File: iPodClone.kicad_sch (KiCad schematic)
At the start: 6 parts, among them U1 V3S, U4 AI12, U5 10104110-0001LF

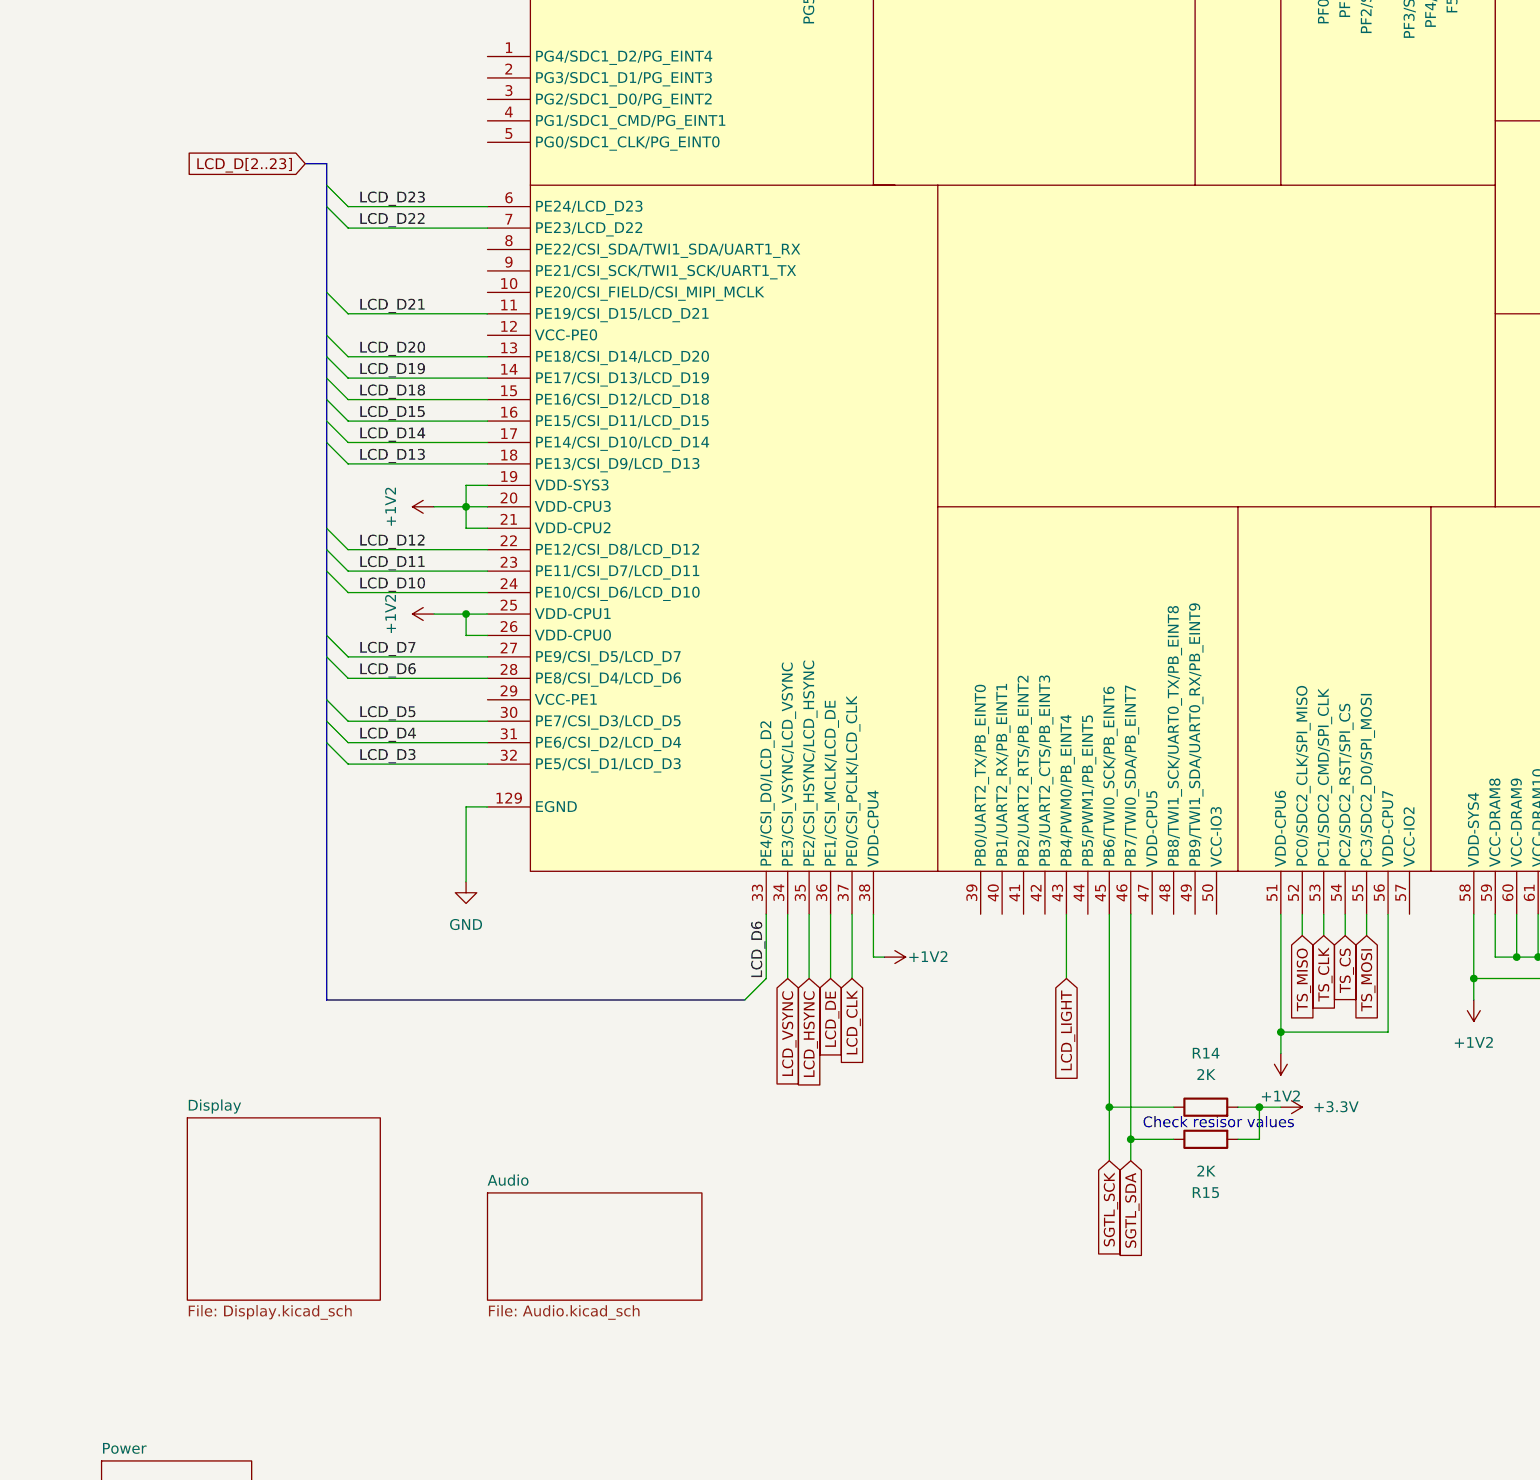
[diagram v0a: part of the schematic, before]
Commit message: power changes, audio changes, testing layout
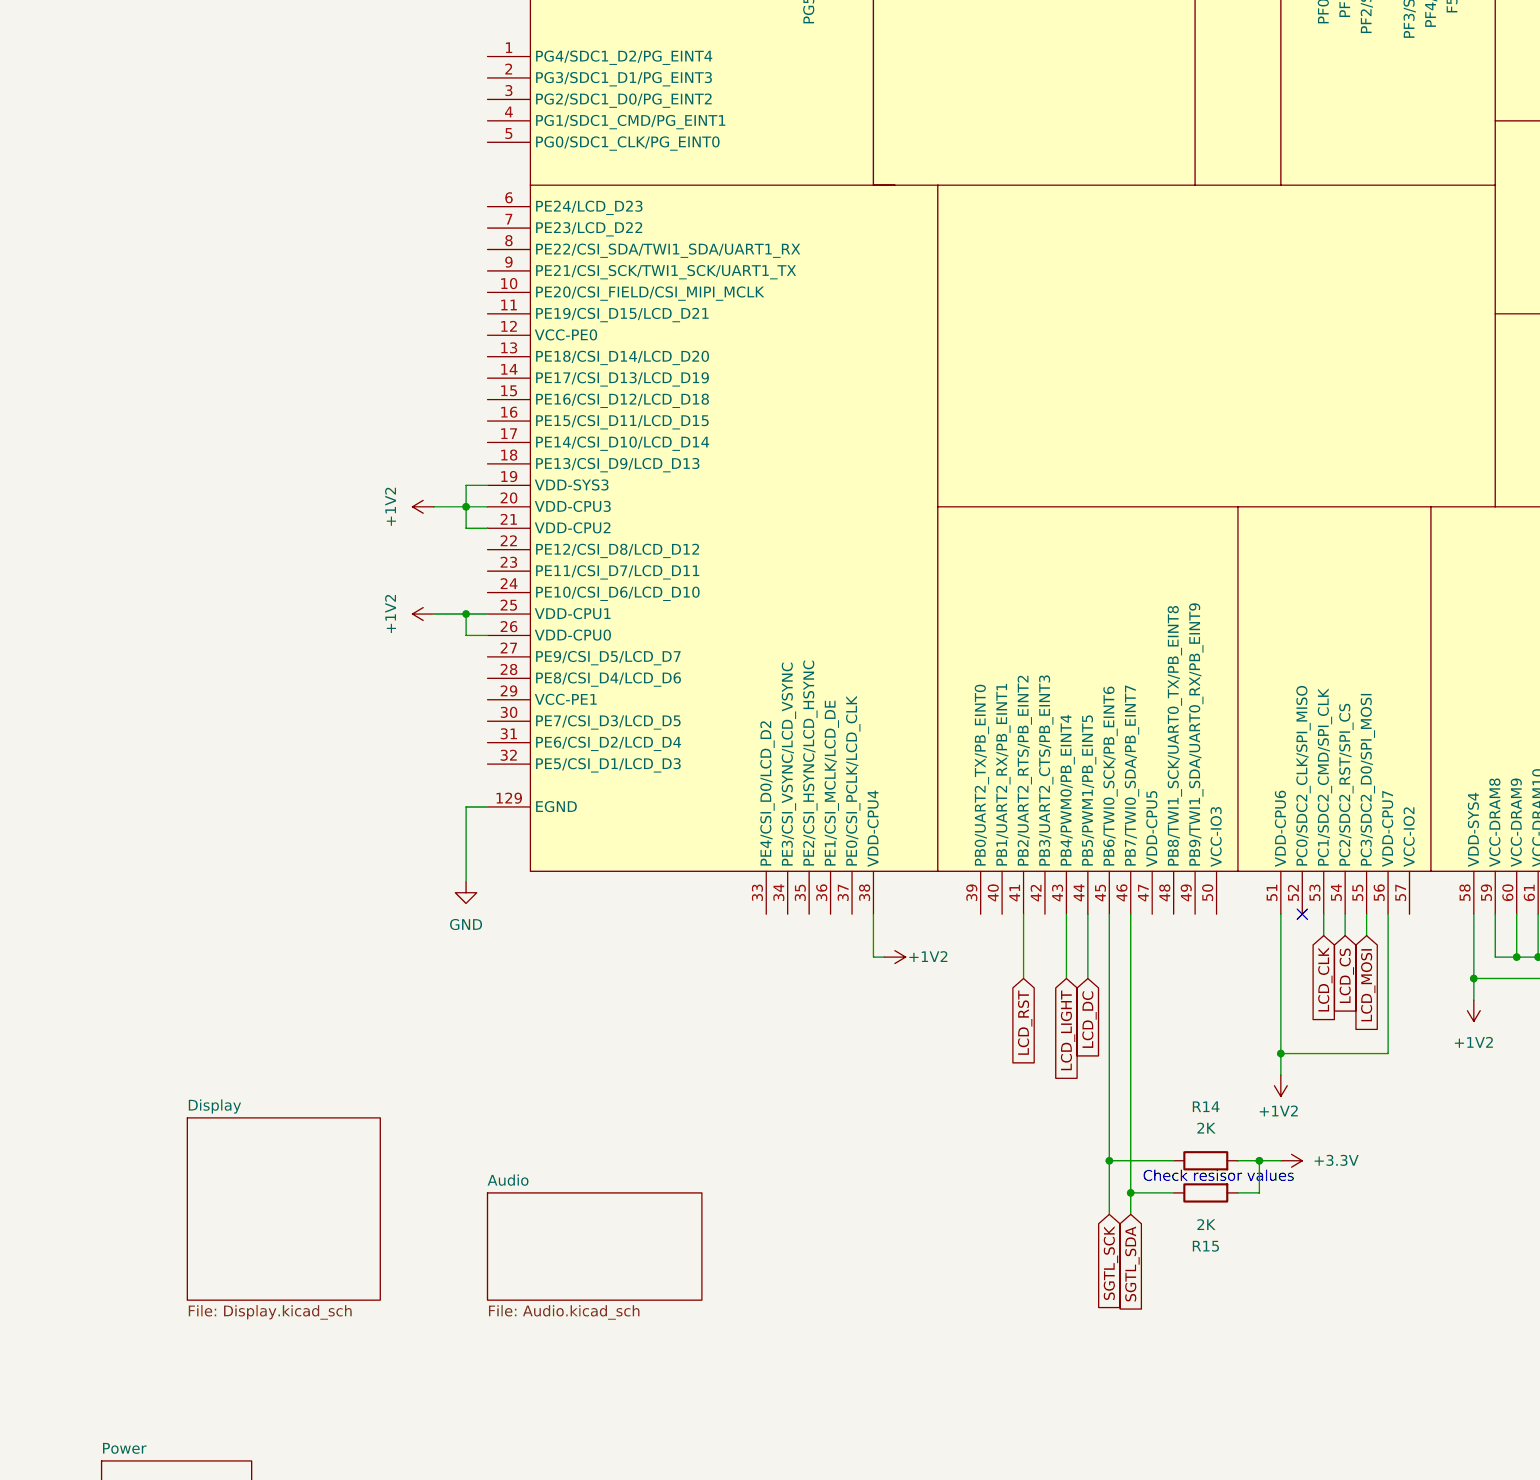
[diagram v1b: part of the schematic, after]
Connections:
- net TS_CLK is gone; now on net LCD_CLK: U1.53 (PC1/SDC2_CMD/SPI_CLK)
- net LCD_CLK: no longer U1.37 (PE0/CSI_PCLK/LCD_CLK)
- net LCD_RST: now reaches U1.41 (PB2/UART2_RTS/PB_EINT2)
- net LCD_DC: now reaches U1.44 (PB5/PWM1/PB_EINT5)
- net LCD_D10: no longer names the net of U1.24 (PE10/CSI_D6/LCD_D10)
- net LCD_D11: no longer names the net of U1.23 (PE11/CSI_D7/LCD_D11)
- net LCD_D12: no longer names the net of U1.22 (PE12/CSI_D8/LCD_D12)
- net LCD_D13: no longer names the net of U1.18 (PE13/CSI_D9/LCD_D13)
- net LCD_D14: no longer names the net of U1.17 (PE14/CSI_D10/LCD_D14)
- net LCD_D15: no longer names the net of U1.16 (PE15/CSI_D11/LCD_D15)
- net LCD_D18: no longer names the net of U1.15 (PE16/CSI_D12/LCD_D18)
- net LCD_D19: no longer names the net of U1.14 (PE17/CSI_D13/LCD_D19)
- net LCD_D20: no longer names the net of U1.13 (PE18/CSI_D14/LCD_D20)
- net LCD_D21: no longer names the net of U1.11 (PE19/CSI_D15/LCD_D21)
- net LCD_D22: no longer names the net of U1.7 (PE23/LCD_D22)
- net LCD_D23: no longer names the net of U1.6 (PE24/LCD_D23)
- net LCD_D3: no longer names the net of U1.32 (PE5/CSI_D1/LCD_D3)
- net LCD_D4: no longer names the net of U1.31 (PE6/CSI_D2/LCD_D4)
- net LCD_D5: no longer names the net of U1.30 (PE7/CSI_D3/LCD_D5)
- net LCD_D6: no longer names the net of U1.28 (PE8/CSI_D4/LCD_D6)
- net LCD_D6: no longer U1.33 (PE4/CSI_D0/LCD_D2)
- net LCD_D7: no longer names the net of U1.27 (PE9/CSI_D5/LCD_D7)
- net LCD_DE: no longer names the net of U1.36 (PE1/CSI_MCLK/LCD_DE)
- net LCD_HSYNC: no longer names the net of U1.35 (PE2/CSI_HSYNC/LCD_HSYNC)
- net LCD_VSYNC: no longer names the net of U1.34 (PE3/CSI_VSYNC/LCD_VSYNC)
- net TS_CS renamed LCD_CS
- net TS_MISO: no longer names the net of U1.52 (PC0/SDC2_CLK/SPI_MISO)
- net TS_MOSI renamed LCD_MOSI
- no-connect marks 0 -> 1
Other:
- moved on the sheet: R14, R15

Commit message: audio changes, better layout
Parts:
- added R11, R12, R13, R19, R20: 10K, symbol Device:R
- added R21: 47K, symbol Device:R
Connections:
- net +3.3V: now also Card1.4 (VDD), R11.1, R12.1, R13.1, R19.1, R20.1, R21.1
- net SDC0_CMD: now also R13.2
- net SDC0_D0: now also R12.2
- net SDC0_D1: now also R11.2
- net SDC0_D2: now also R20.2
- net SDC0_D3: now also R19.2
- net PCM_CS: now reaches U1.37 (PE0/CSI_PCLK/LCD_CLK)
- net at U5.4 (ID): now also R21.2
- net LCD_CLK renamed SPI_CLK
- net LCD_MOSI renamed SPI_MOSI
- no-connect marks 1 -> 2
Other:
- moved on the sheet: Card1

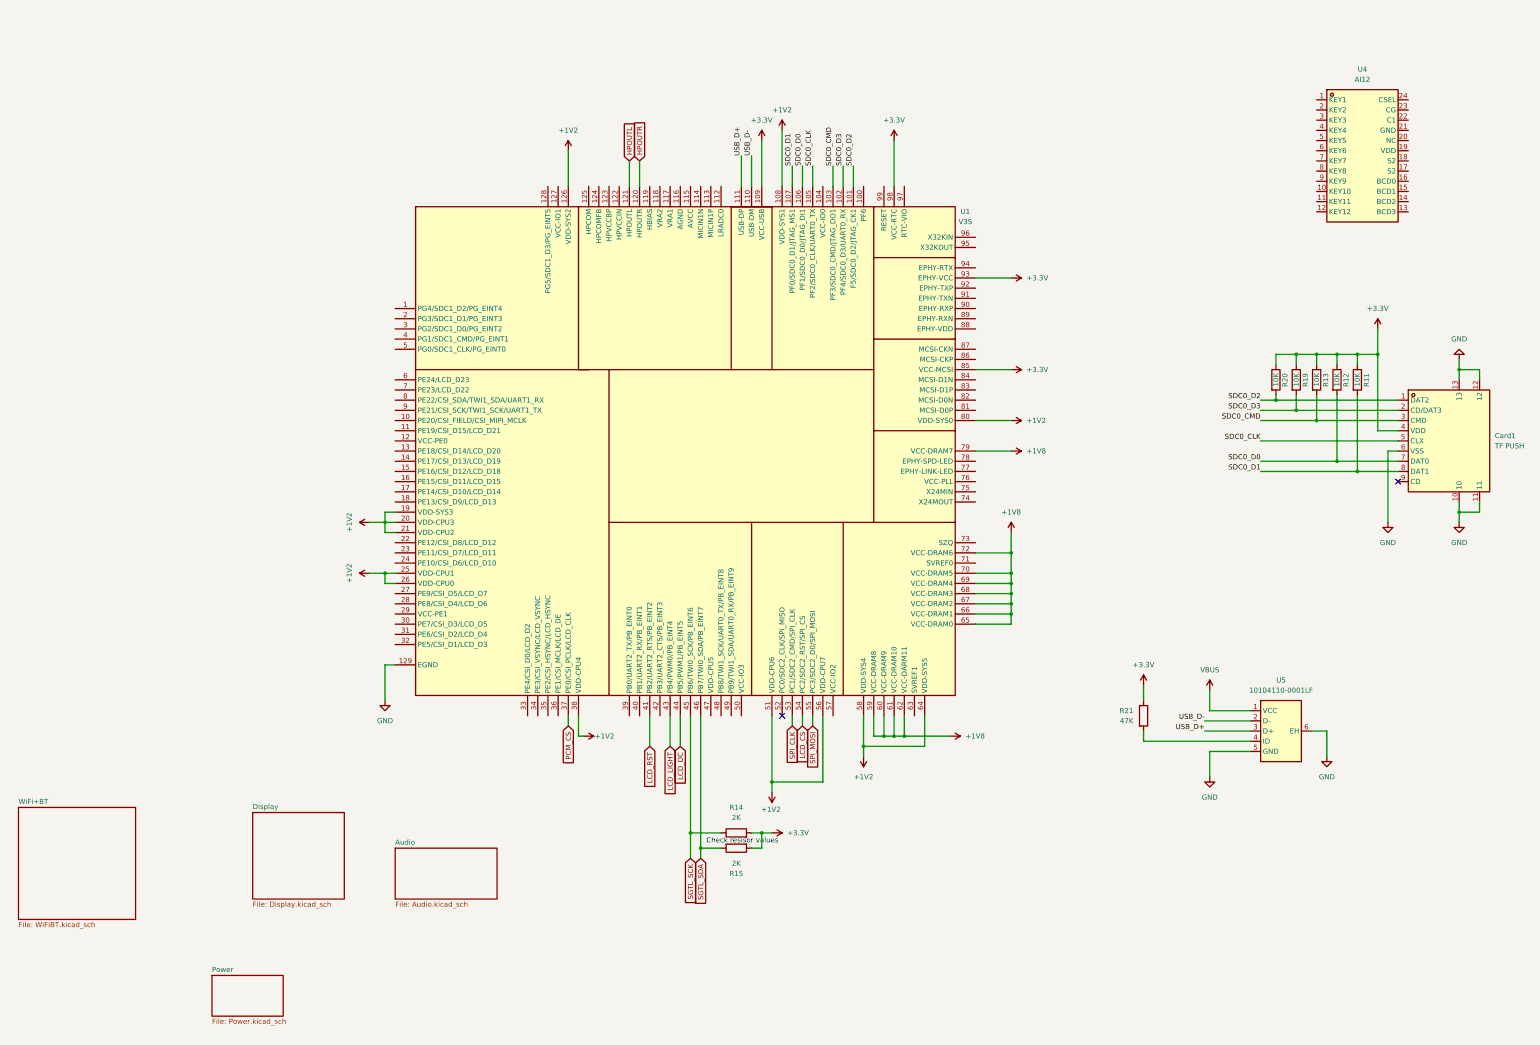
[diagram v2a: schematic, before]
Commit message: power changes to v3s, nand
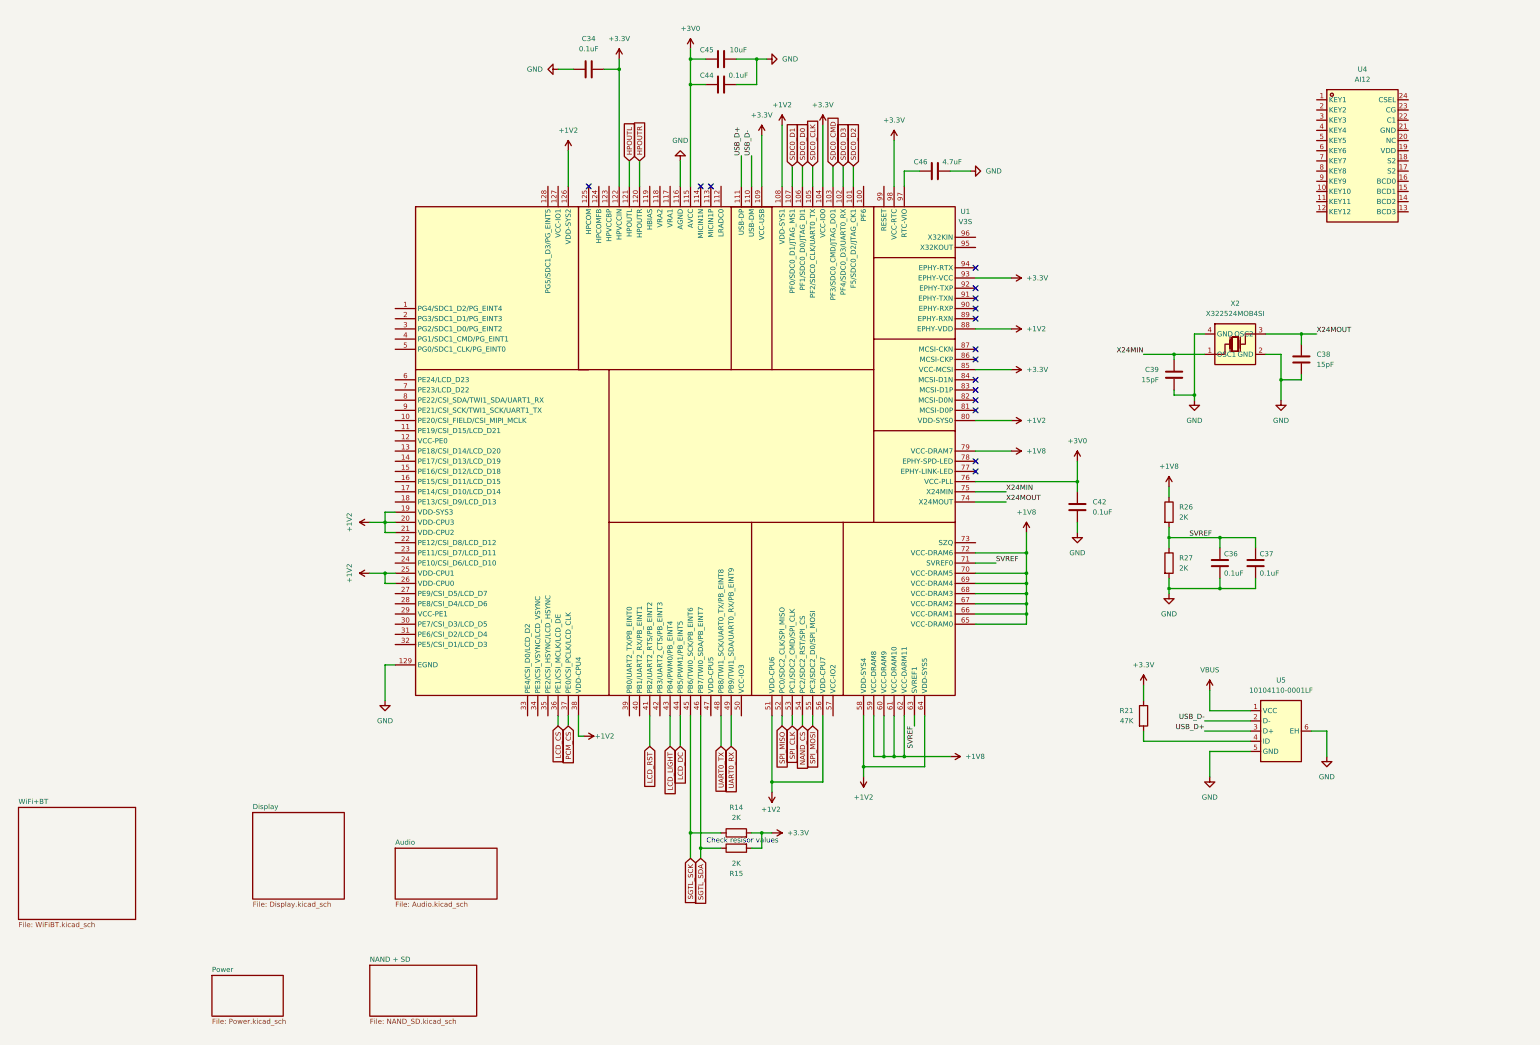
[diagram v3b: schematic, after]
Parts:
- removed Card1: TF PUSH, easyeda2kicad:TF-SMD_TF-PUSH, symbol easyeda2kicad:TFPUSH
- removed R11, R12, R13, R19, R20: 10K, symbol Device:R
- added C34, C36, C37, C42, C44: 0.1uF, symbol Device:C
- added C38, C39: 15pF, symbol Device:C
- added C45: 10uF, symbol Device:C
- added C46: 4.7uF, symbol Device:C
- added R26, R27: 2K, symbol Device:R
- added X2: X322524MOB4SI, easyeda2kicad:CRYSTAL-SMD_4P-L3.2-W2.5-BL, symbol easyeda2kicad:X322524MOB4SI
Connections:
- net +1V2: now also U1.88 (EPHY-VDD)
- net +1V8: now also R26.1
- net +3.3V: now also U1.104 (VCC-IO0), U1.122 (HPVCCIN), C34.1
- net GND: now also U1.116 (AGND), C34.2, C36.2, C37.2, C38.2, C39.2, C42.2, C44.1, C45.1, C46.1, R27.2, X2.2 (GND), X2.4 (GND)
- net LCD_CS: now also U1.36 (PE1/CSI_MCLK/LCD_DE); no longer U1.54 (PC2/SDC2_RST/SPI_CS)
- net +3V0: now reaches U1.115 (AVCC)
- net +3V0: now also U1.76 (VCC-PLL), C42.1, C44.2, C45.2
- net UART0_TX: now reaches U1.48 (PB8/TWI1_SCK/UART0_TX/PB_EINT8)
- net UART0_RX: now reaches U1.49 (PB9/TWI1_SDA/UART0_RX/PB_EINT9)
- net SPI_MISO: now reaches U1.52 (PC0/SDC2_CLK/SPI_MISO)
- net SVREF: now reaches U1.63 (SVREF1)
- net SVREF: now also U1.71 (SVREF0), C36.1, C37.1, R26.2, R27.1
- net X24MOUT: now reaches U1.74 (X24MOUT)
- net X24MOUT: now also C38.1, X2.3 (OSC2)
- net X24MIN: now reaches U1.75 (X24MIN)
- net X24MIN: now also C39.1, X2.1 (OSC1)
- net at U1.97 (RTC-VIO): now also C46.2
- new net NAND_CS: U1.54 (PC2/SDC2_RST/SPI_CS)
- no-connect marks 2 -> 16
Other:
- added sheet NAND + SD (NAND_SD.kicad_sch)

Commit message: power changes for v3s, cleanup
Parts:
- removed U4: AI12, easyeda2kicad:SSOP-24_L8.8-W4.0-P0.64-LS6.2-BL, symbol easyeda2kicad:AI12
- added C43, C49: 18pF, symbol Device:C
- added C47, C48: 0.1uF, symbol Device:C
- added R28: 200K, symbol Device:R
- added R29: 10M, symbol Device:R
- added X1: FC-12M32.768KHZ7PF20PPM, easyeda2kicad:FC-12M_L2.0-W1.2, symbol easyeda2kicad:FC-12M32.768KHZ7PF20PPM
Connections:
- net +3.3V: now also U1.12 (VCC-PE0), U1.127 (VCC-IO1), U1.29 (VCC-PE1), U1.50 (VCC-IO3), U1.57 (VCC-IO2)
- net GND: now also C43.2, C47.1, C48.2, C49.2, R28.1
- net at U1.117 (VRA1): now also C47.2
- net at U1.118 (VRA2): now also C48.1, R28.2
- net X32KOUT: now reaches U1.95 (X32KOUT)
- net X32KOUT: now also C49.1, R29.2, X1.2 (OSC2)
- net X32KIN: now reaches U1.96 (X32KIN)
- net X32KIN: now also C43.1, R29.1, X1.1 (OSC1)
- no-connect marks 16 -> 42
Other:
- note added: "USB"
- title: (none) -> iPodClone
- moved on the sheet: C34, C42, C44, C45, C46, R14, R15, R21, U1, U5

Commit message: gitignore and audio changes
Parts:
- added C15: 0.1uF, symbol Device:C
- added JP3: SolderJumper_2_Open, symbol Jumper:SolderJumper_2_Open
- added R32: 240, symbol Device:R
- added R34: 10K, symbol Device:R
- added TP1, TP2: TestPoint, symbol Connector:TestPoint
- R14, R15: value 2K -> 5.1K
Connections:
- net +3.3V: now also R34.1
- net GND: now also C15.2, JP3.1 (A), R32.2
- net UART0_RX: now also TP1.1
- net UART0_TX: now also TP2.1
- net GPOUT: now reaches U1.35 (PE2/CSI_HSYNC/LCD_HSYNC)
- net at U1.73 (SZQ): now also R32.1
- net V3S-ESP32_RX: now reaches U1.8 (PE22/CSI_SDA/TWI1_SDA/UART1_RX)
- net V3S-ESP32_TX: now reaches U1.9 (PE21/CSI_SCK/TWI1_SCK/UART1_TX)
- net RESET: now reaches U1.99 (RESET)
- net RESET: now also C15.1, JP3.2 (B), R34.2
- net SGTL_SCK renamed I2C_SCK
- net SGTL_SDA renamed I2C_SDA
- no-connect marks 42 -> 48
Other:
- note removed: "Check resisor values"
